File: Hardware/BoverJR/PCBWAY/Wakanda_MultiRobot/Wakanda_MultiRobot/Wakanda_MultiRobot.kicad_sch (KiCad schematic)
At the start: 26 parts, among them J1 Alimentacion, J10 I2C, J14 RANDOM, J2 Conn_01X03, J3 Sensor Distancia 1, J3 TATAMI Frontal Derecho, J4 Conn_01X03, J4 TATAMI Frontal Izquierdo, J5 Conn_01X03, J6 Conn_01X03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

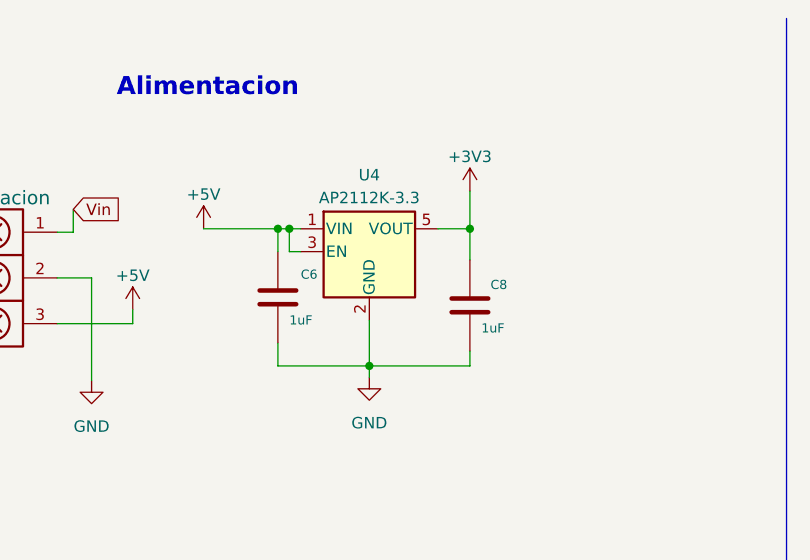
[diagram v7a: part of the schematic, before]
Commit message: debo cambiar regulador ap21 3v3 por ams1117 3v3 lpm
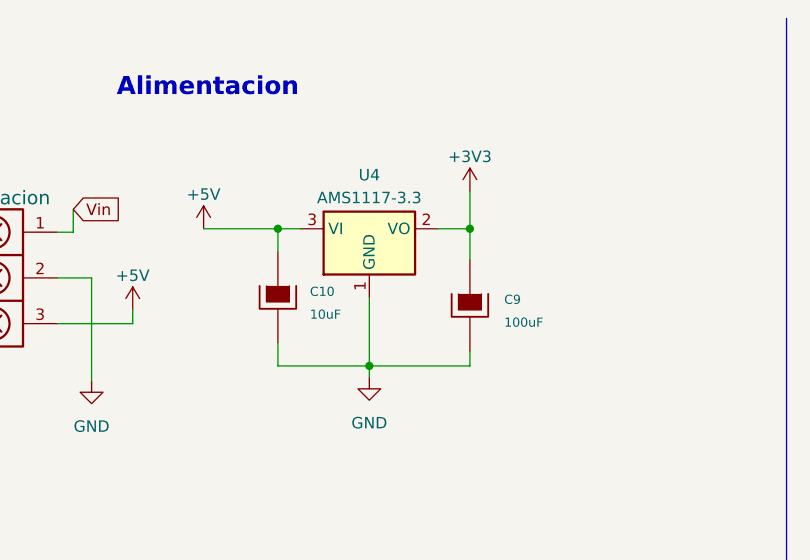
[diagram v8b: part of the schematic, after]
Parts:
- removed C6, C8: 1uF, EESTN5:C_0805, symbol EESTN5:C
- removed U4: AP2112K-3.3, Package_TO_SOT_SMD:SOT-23-5, symbol Regulator_Linear:AP2112K-3.3
- added C10: 10uF, Capacitor_THT:CP_Axial_L10.0mm_D4.5mm_P15.00mm_Horizontal, symbol EESTN5:CAPAPOL
- added C9: 100uF, Capacitor_THT:CP_Axial_L10.0mm_D4.5mm_P15.00mm_Horizontal, symbol EESTN5:CAPAPOL
- added U4: AMS1117-3.3, Package_TO_SOT_SMD:SOT-223-3_TabPin2, symbol Regulator_Linear:AMS1117-3.3
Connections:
- net +3V3: now also C9.1, U4.2 (VO)
- net +5V: now also C10.1, U4.3 (VI)
- net GND: now also C10.2, C9.2, U4.1 (GND)
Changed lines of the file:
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@@
   (junction (at 216.027 21.336) (diameter 0) (color 0 0 0 0)
   )
-  (junction (at 54.864 35.179) (diameter 0) (color 0 0 0 0)
-  )
   (junction (at 187.96 42.037) (diameter 0) (color 0 0 0 0)
   )
@@
     (stroke (width 0) (type default))
   )
-  (wire (pts (xy 56.134 37.719) (xy 54.864 37.719))
-    (stroke (width 0) (type default))
-  )
   (wire (pts (xy 216.535 53.594) (xy 219.075 53.594))
     (stroke (width 0) (type default))
@@
     (stroke (width 0) (type default))
   )
-  (wire (pts (xy 53.594 35.179) (xy 54.864 35.179))
-    (stroke (width 0) (type default))
-  )
   (wire (pts (xy 208.915 21.336) (xy 216.027 21.336))
     (stroke (width 0) (type default))
@@
     (stroke (width 0) (type default))
   )
-  (wire (pts (xy 63.754 45.339) (xy 63.754 50.419))
+  (wire (pts (xy 63.754 42.799) (xy 63.754 50.419))
     (stroke (width 0) (type default))
   )
@@
     (stroke (width 0) (type default))
   )
-  (wire (pts (xy 54.864 35.179) (xy 56.134 35.179))
-    (stroke (width 0) (type default))
-  )
-  (wire (pts (xy 54.864 37.719) (xy 54.864 35.179))
+  (wire (pts (xy 53.594 35.179) (xy 56.134 35.179))
     (stroke (width 0) (type default))
   )
@@
     )
   )
+  (symbol (lib_id "Regulator_Linear:AMS1117-3.3") (at 63.754 35.179 0) (unit 1)
+    (in_bom yes) (on_board yes) (dnp no) (fields_autoplaced)
+    (property "Reference" "U4" (at 63.754 29.21 0)
+      (effects (font (size 1.27 1.27)))
+    )
+    (property "Value" "AMS1117-3.3" (at 63.754 31.75 0)
+      (effects (font (size 1.27 1.27)))
+    )
+    (property "Footprint" "Package_TO_SOT_SMD:SOT-223-3_TabPin2" (at 63.754 30.099 0)
+      (effects (font (size 1.27 1.27)) hide)
+    )
+    (property "Datasheet" "http://www.advanced-monolithic.com/pdf/ds1117.pdf" (at 66.294 41.529 0)
+      (effects (font (size 1.27 1.27)) hide)
+    )
+    (pin "1")
+    (pin "2")
+    (pin "3")
+    (instances
+      (project "Wakanda_MultiRobot"
+        (path "/7706e104-9d42-4651-8ea1-0974927a2230"
+          (reference "U4") (unit 1)
+        )
+      )
+    )
+  )
   (symbol (lib_id "EESTN5:Conn_01X03") (at 108.204 133.35 0) (unit 1)
     (in_bom yes) (on_board yes) (dnp no) (fields_autoplaced)
@@
     )
   )
-  (symbol (lib_id "EESTN5:C") (at 74.93 43.688 0) (unit 1)
-    (in_bom yes) (on_board yes) (dnp no)
-    (property "Reference" "C8" (at 77.216 41.402 0)
-      (effects (font (size 1.016 1.016)) (justify left))
-    )
-    (property "Value" "1uF" (at 76.2 46.228 0)
-      (effects (font (size 1.016 1.016)) (justify left))
-    )
-    (property "Footprint" "EESTN5:C_0805" (at 75.8952 47.498 0)
-      (effects (font (size 0.762 0.762)) hide)
-    )
-    (property "Datasheet" "" (at 74.93 43.688 0)
-      (effects (font (size 1.524 1.524)))
-    )
-    (pin "1")
-    (pin "2")
-    (instances
-      (project "wakanda-board"
-        (path "/19267798-4e4c-4aeb-bec3-b7452995418d"
-          (reference "C8") (unit 1)
-        )
-      )
-      (project "Wakanda_MultiRobot"
-        (path "/7706e104-9d42-4651-8ea1-0974927a2230"
-          (reference "C6") (unit 1)
-        )
-      )
-      (project "PCB-Mando-Radiocontrol-backups"
-        (path "/a09d701e-8048-4e72-8e3a-cb0f8f921380"
-          (reference "C8") (unit 1)
-        )
-      )
-      (project "PCB-Controladora-Vuelo"
-        (path "/ac5864b2-231c-45bd-8efa-594ea27cde2d"
-          (reference "C7") (unit 1)
-        )
-      )
-      (project "Esp32Modulo"
-        (path "/d8ce7d9a-219e-40d1-b957-d72bdccbdc30"
-          (reference "C4") (unit 1)
-        )
-      )
-    )
-  )
-  (symbol (lib_id "Regulator_Linear:AP2112K-3.3") (at 63.754 37.719 0) (unit 1)
-    (in_bom yes) (on_board yes) (dnp no) (fields_autoplaced)
-    (property "Reference" "U4" (at 63.754 29.21 0)
-      (effects (font (size 1.27 1.27)))
-    )
-    (property "Value" "AP2112K-3.3" (at 63.754 31.75 0)
-      (effects (font (size 1.27 1.27)))
-    )
-    (property "Footprint" "Package_TO_SOT_SMD:SOT-23-5" (at 63.754 29.464 0)
-      (effects (font (size 1.27 1.27)) hide)
-    )
-    (property "Datasheet" "https://www.diodes.com/assets/Datasheets/AP2112.pdf" (at 63.754 35.179 0)
-      (effects (font (size 1.27 1.27)) hide)
-    )
-    (pin "1")
-    (pin "2")
-    (pin "3")
-    (pin "4")
-    (pin "5")
-    (instances
-      (project "Wakanda_MultiRobot"
-        (path "/7706e104-9d42-4651-8ea1-0974927a2230"
-          (reference "U4") (unit 1)
-        )
-      )
-    )
-  )
   (symbol (lib_name "+5V_1") (lib_id "power:+5V") (at 45.339 35.179 0) (unit 1)
     (in_bom yes) (on_board yes) (dnp no) (fields_autoplaced)
@@
     )
   )
-  (symbol (lib_id "EESTN5:C") (at 53.594 42.799 0) (unit 1)
-    (in_bom yes) (on_board yes) (dnp no)
-    (property "Reference" "C6" (at 56.134 40.259 0)
-      (effects (font (size 1.016 1.016)) (justify left))
-    )
-    (property "Value" "1uF" (at 54.864 45.339 0)
-      (effects (font (size 1.016 1.016)) (justify left))
-    )
-    (property "Footprint" "EESTN5:C_0805" (at 54.5592 46.609 0)
-      (effects (font (size 0.762 0.762)) hide)
-    )
-    (property "Datasheet" "" (at 53.594 42.799 0)
-      (effects (font (size 1.524 1.524)))
-    )
-    (pin "1")
-    (pin "2")
-    (instances
-      (project "wakanda-board"
-        (path "/19267798-4e4c-4aeb-bec3-b7452995418d"
-          (reference "C6") (unit 1)
-        )
-      )
-      (project "Wakanda_MultiRobot"
-        (path "/7706e104-9d42-4651-8ea1-0974927a2230"
-          (reference "C5") (unit 1)
-        )
-      )
-      (project "PCB-Mando-Radiocontrol-backups"
-        (path "/a09d701e-8048-4e72-8e3a-cb0f8f921380"
-          (reference "C6") (unit 1)
-        )
-      )
-      (project "PCB-Controladora-Vuelo"
-        (path "/ac5864b2-231c-45bd-8efa-594ea27cde2d"
-          (reference "C3") (unit 1)
-        )
-      )
-      (project "Esp32Modulo"
-        (path "/d8ce7d9a-219e-40d1-b957-d72bdccbdc30"
-          (reference "C2") (unit 1)
-        )
-      )
-    )
-  )
   (symbol (lib_name "+5V_1") (lib_id "power:+5V") (at 65.659 93.091 0) (unit 1)
     (in_bom yes) (on_board yes) (dnp no) (fields_autoplaced)
@@
     )
   )
+  (symbol (lib_id "EESTN5:CAPAPOL") (at 53.594 42.799 0) (unit 1)
+    (in_bom yes) (on_board yes) (dnp no) (fields_autoplaced)
+    (property "Reference" "C10" (at 57.15 42.164 0)
+      (effects (font (size 1.016 1.016)) (justify left))
+    )
+    (property "Value" "10uF" (at 57.15 44.704 0)
+      (effects (font (size 1.016 1.016)) (justify left))
+    )
+    (property "Footprint" "Capacitor_THT:CP_Axial_L10.0mm_D4.5mm_P15.00mm_Horizontal" (at 56.134 46.609 0)
+      (effects (font (size 0.762 0.762)) hide)
+    )
+    (property "Datasheet" "" (at 53.594 42.799 0)
+      (effects (font (size 7.62 7.62)))
+    )
+    (pin "1")
+    (pin "2")
+    (instances
+      (project "Wakanda_MultiRobot"
+        (path "/7706e104-9d42-4651-8ea1-0974927a2230"
+          (reference "C10") (unit 1)
+        )
+      )
+    )
+  )
   (symbol (lib_id "2018---MiniSumo---NANO---DRV8872-rescue:Mounting_Hole-EESTN51") (at 279.019 27.178 0) (unit 1)
     (in_bom yes) (on_board yes) (dnp no)
@@
         )
       )
+    )
+  )
+  (symbol (lib_id "EESTN5:CAPAPOL") (at 74.93 43.688 0) (unit 1)
+    (in_bom yes) (on_board yes) (dnp no) (fields_autoplaced)
+    (property "Reference" "C9" (at 78.74 43.053 0)
+      (effects (font (size 1.016 1.016)) (justify left))
+    )
+    (property "Value" "100uF" (at 78.74 45.593 0)
+      (effects (font (size 1.016 1.016)) (justify left))
+    )
+    (property "Footprint" "Capacitor_THT:CP_Axial_L10.0mm_D4.5mm_P15.00mm_Horizontal" (at 77.47 47.498 0)
+      (effects (font (size 0.762 0.762)) hide)
+    )
+    (property "Datasheet" "" (at 74.93 43.688 0)
+      (effects (font (size 7.62 7.62)))
+    )
+    (pin "1")
+    (pin "2")
+    (instances
+      (project "Wakanda_MultiRobot"
+        (path "/7706e104-9d42-4651-8ea1-0974927a2230"
+          (reference "C9") (unit 1)
+        )
+      )
